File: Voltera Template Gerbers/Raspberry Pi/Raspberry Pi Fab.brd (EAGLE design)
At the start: 65 x 56 mm, 1 part

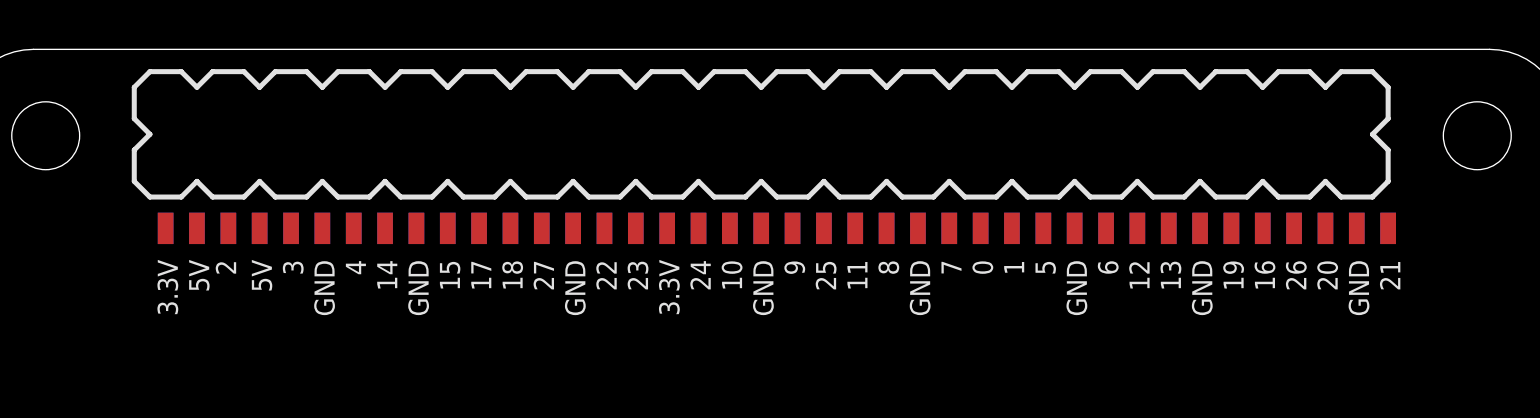
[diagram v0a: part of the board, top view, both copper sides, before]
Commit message: Created 2x3 and 3x4 FR1 templates. Added 'fab' version of the templates
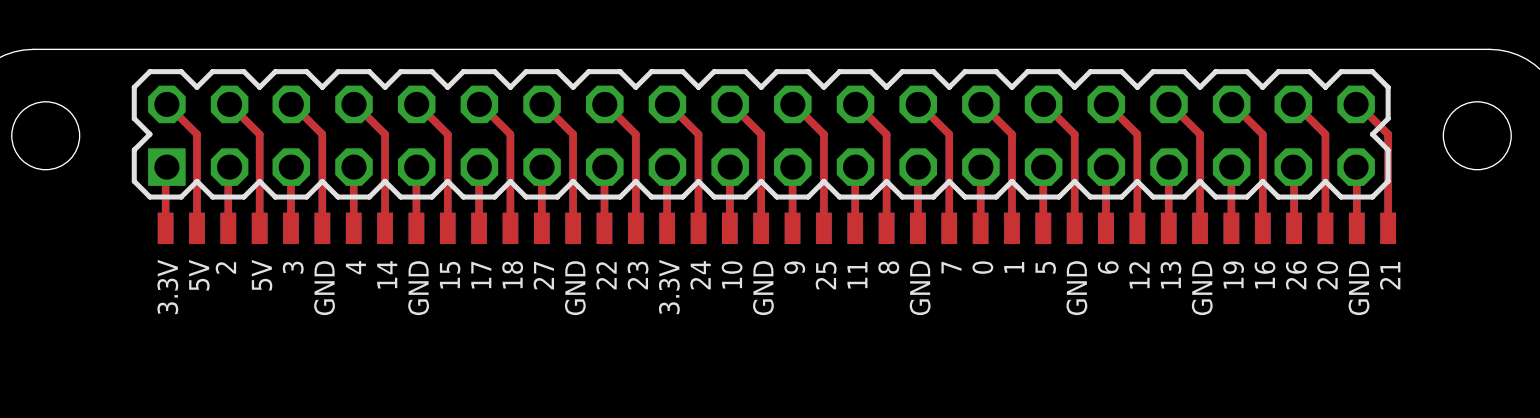
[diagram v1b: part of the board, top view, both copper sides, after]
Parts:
- removed E$1: (no value), voltera_community_lib:PI_HAT
- added E$2: (no value), voltera_EAGLE_community_lib:PI_HAT_RAW
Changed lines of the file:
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@@
 </autorouter>
 <elements>
-<element name="E$1" library="voltera_community_lib" package="PI_HAT" value="" x="0" y="0"/>
+<element name="E$2" library="voltera_EAGLE_community_lib" package="PI_HAT_RAW" value="" x="0" y="0"/>
 </elements>
 <signals>
